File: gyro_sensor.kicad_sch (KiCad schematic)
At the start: 4 parts, among them U5_1 ICM-42688-P

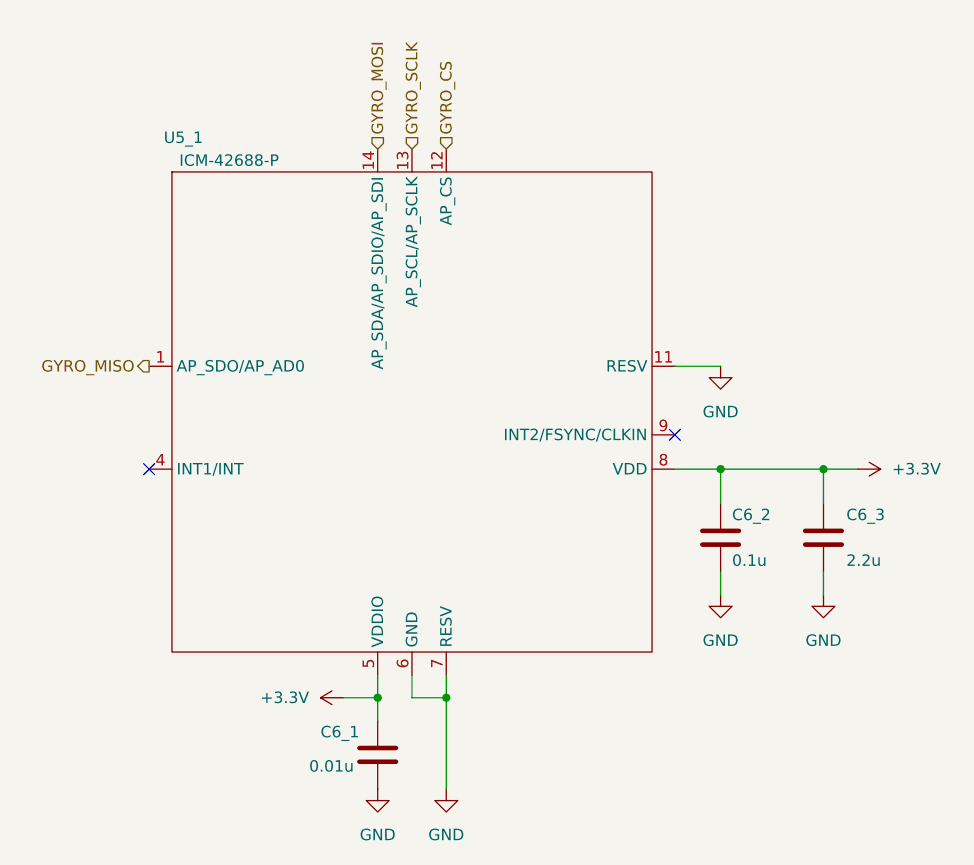
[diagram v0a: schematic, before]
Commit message: コンデンサの表記を統一
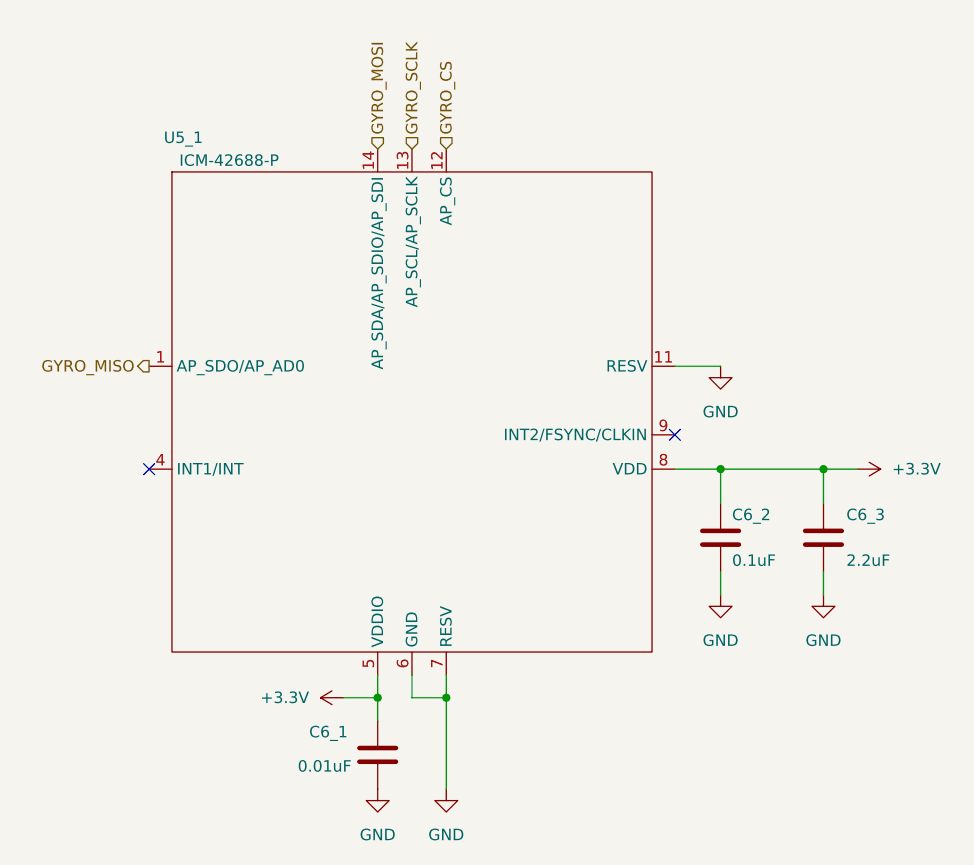
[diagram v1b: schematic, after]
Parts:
- C6_1: value 0.01u -> 0.01uF
- C6_2: value 0.1u -> 0.1uF
- C6_3: value 2.2u -> 2.2uF
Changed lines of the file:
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@@
   (symbol (lib_id "Device:C") (at 138.43 130.81 0) (unit 1)
     (in_bom yes) (on_board yes) (dnp no)
-    (property "Reference" "C6_1" (at 132.08 128.27 0)
-      (effects (font (size 1.27 1.27)) (justify left))
-    )
-    (property "Value" "0.01u" (at 130.81 132.08 0)
+    (property "Reference" "C6_1" (at 130.81 128.27 0)
+      (effects (font (size 1.27 1.27)) (justify left))
+    )
+    (property "Value" "0.01uF" (at 129.54 132.08 0)
       (effects (font (size 1.27 1.27)) (justify left))
     )
@@
       (effects (font (size 1.27 1.27)) (justify left))
     )
-    (property "Value" "2.2u" (at 190.5 109.22 0)
+    (property "Value" "2.2uF" (at 190.5 109.22 0)
       (effects (font (size 1.27 1.27)) (justify left))
     )
@@
       (effects (font (size 1.27 1.27)) (justify left))
     )
-    (property "Value" "0.1u" (at 177.8 109.22 0)
-      (effects (font (size 1.27 1.27)) (justify left))
-    )
+    (property "Value" "0.1uF" (at 177.8 109.22 0)
+      (effects (font (size 1.27 1.27)) (justify left))
+    )

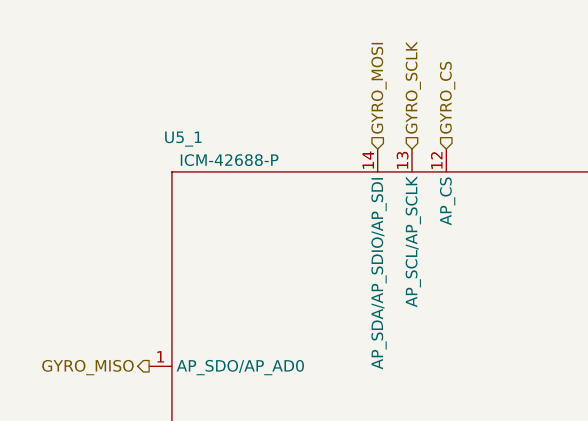
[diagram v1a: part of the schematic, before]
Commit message: ジャイロセンサのアノテーションがモータドライバと重複していたので修正
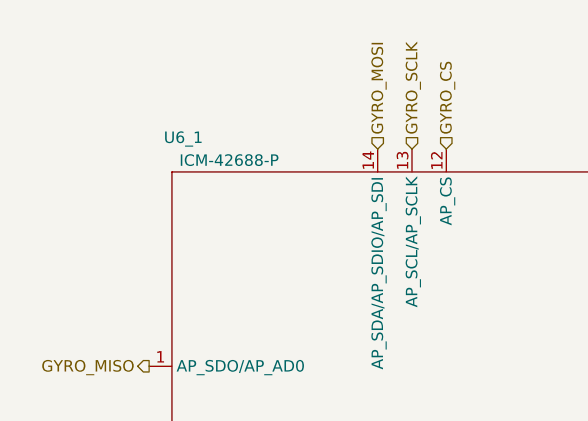
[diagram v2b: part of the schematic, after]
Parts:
- renumbered U5_1 to U6_1
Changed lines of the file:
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@@
   (symbol (lib_id "ICM-42688-P:ICM-42688-P") (at 113.03 63.5 0) (unit 1)
     (in_bom yes) (on_board yes) (dnp no)
-    (property "Reference" "U5_1" (at 116.84 62.23 0)
+    (property "Reference" "U6_1" (at 116.84 62.23 0)
       (effects (font (size 1.27 1.27)))
     )
@@
       (project "fast_respect"
         (path "/588ca8cd-b11b-4b55-96d9-278aac6cd0cf/c0d943d8-7bed-4ffd-b406-edd8b25f7433"
-          (reference "U5_1") (unit 1)
+          (reference "U6_1") (unit 1)
         )
       )

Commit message: アノテーション番号ミスの修正とフットプリント割り当て途中（部品リストも途中生成）
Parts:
- C6_1, C6_2, C6_3: footprint (none) -> Capacitor_SMD:C_0603_1608Metric_Pad1.08x0.95mm_HandSolder
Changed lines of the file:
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@@
       (effects (font (size 1.27 1.27)) (justify left))
     )
-    (property "Footprint" "" (at 139.3952 134.62 0)
+    (property "Footprint" "Capacitor_SMD:C_0603_1608Metric_Pad1.08x0.95mm_HandSolder" (at 139.3952 134.62 0)
       (effects (font (size 1.27 1.27)) hide)
     )
@@
       (effects (font (size 1.27 1.27)) (justify left))
     )
-    (property "Footprint" "" (at 188.9252 110.49 0)
+    (property "Footprint" "Capacitor_SMD:C_0603_1608Metric_Pad1.08x0.95mm_HandSolder" (at 188.9252 110.49 0)
       (effects (font (size 1.27 1.27)) hide)
     )
@@
       (effects (font (size 1.27 1.27)) (justify left))
     )
-    (property "Footprint" "" (at 177.4952 110.49 0)
-      (effects (font (size 1.27 1.27)) hide)
-    )
+    (property "Footprint" "Capacitor_SMD:C_0603_1608Metric_Pad1.08x0.95mm_HandSolder" (at 177.4952 110.49 0)
+      (effects (font (size 1.27 1.27)) hide)
+    )

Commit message: ジャイロとモータドライバのフットプリント作成して登録、シンボルと紐付けた。
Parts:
- U6_1: footprint (none) -> Self-Made_Generic_Packages:LGA-14_ExpandPad_3x2.5mm_P0.5mm_LayoutBorder3x4y
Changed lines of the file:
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@@
       (effects (font (size 1.27 1.27)))
     )
-    (property "Footprint" "" (at 113.03 63.5 0)
+    (property "Footprint" "Self-Made_Generic_Packages:LGA-14_ExpandPad_3x2.5mm_P0.5mm_LayoutBorder3x4y" (at 113.03 63.5 0)
       (effects (font (size 1.27 1.27)) hide)
     )
